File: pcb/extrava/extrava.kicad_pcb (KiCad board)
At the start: 2 copper layers, 38.1 x 40.6 mm, 24 parts, among them J1 Conn_01x01_Socket, J2 Conn_01x01_Socket, J3 Conn_01x01_Socket, J4 Conn_01x01_Socket, U1 XIAO_ESP32C3, U2 AD5941BCPZ, Y1 ABM8-16.000MHZ-10-1-U-T

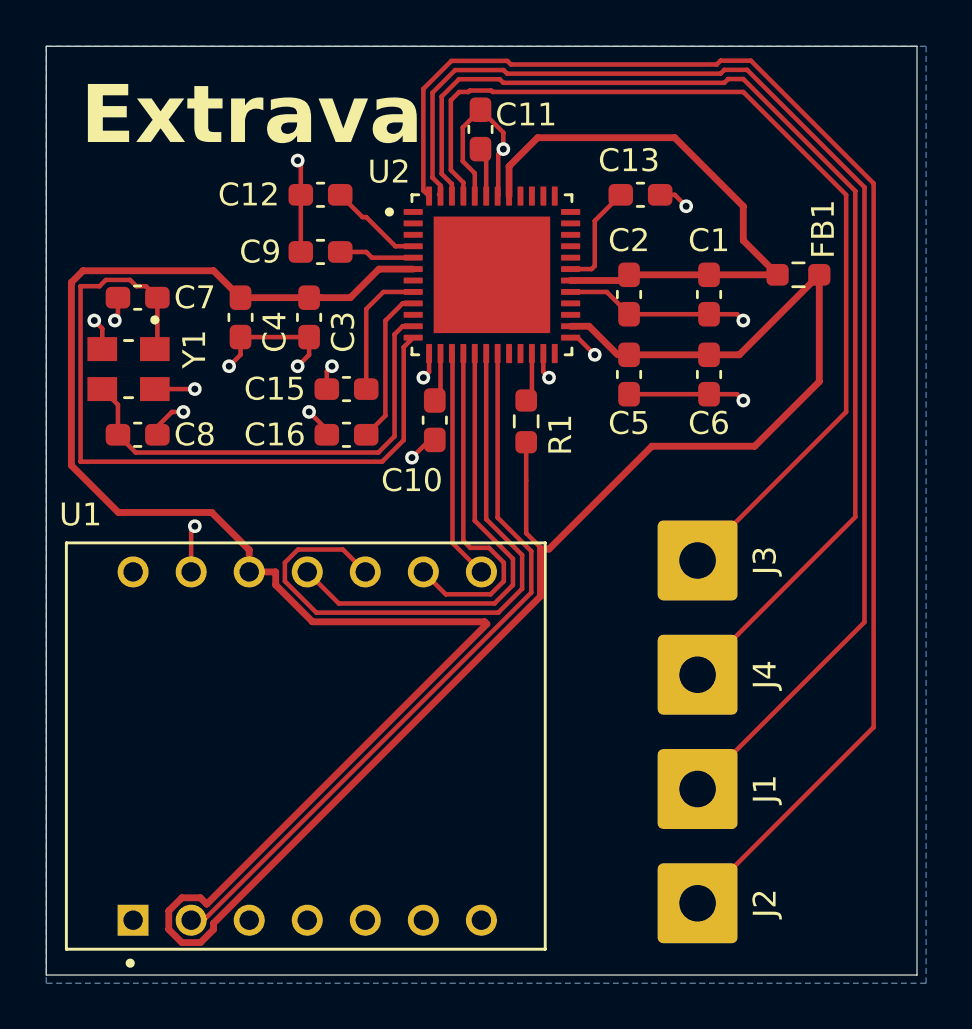
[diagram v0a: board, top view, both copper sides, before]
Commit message: fix(layout): closer decoupling caps
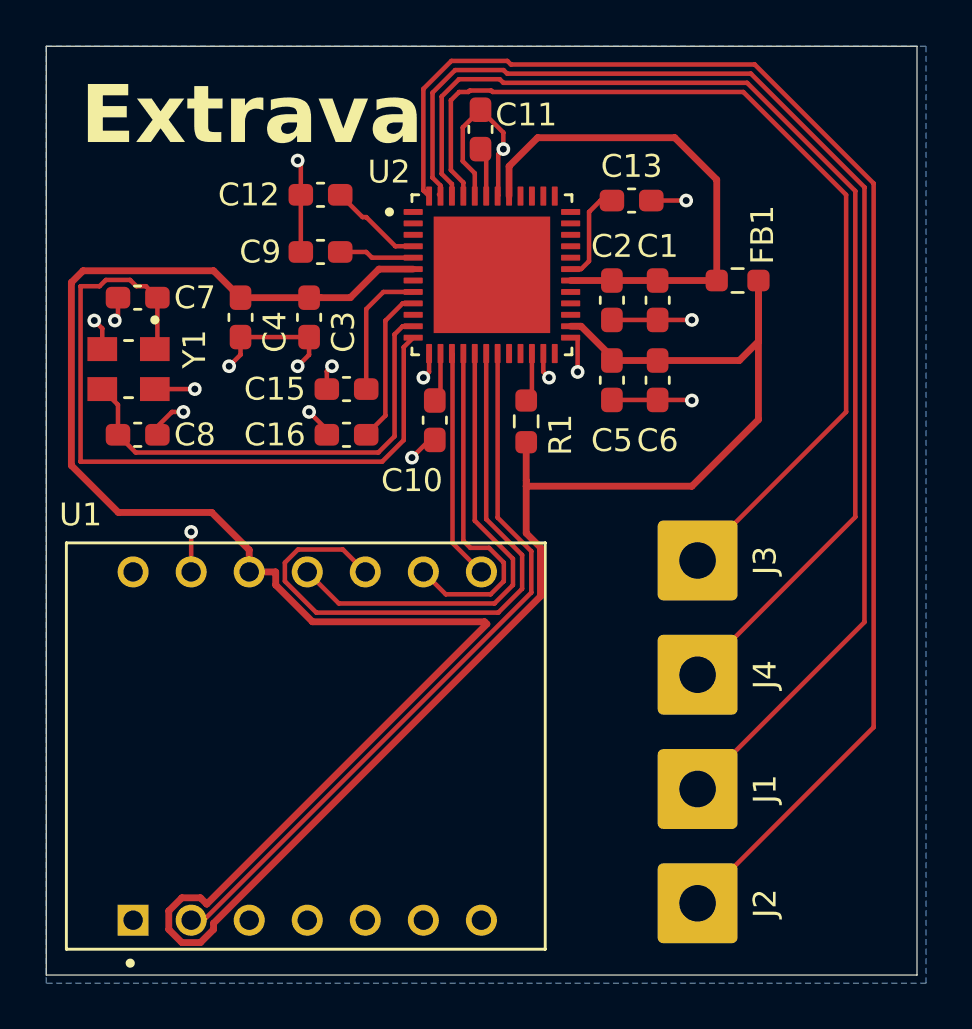
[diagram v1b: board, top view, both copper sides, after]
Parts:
- moved FB1 2.67 mm to (113.5, 53.0)
- moved C1 2.26 mm to (110.0, 53.9)
- moved C6 2.26 mm to (110.0, 57.4)
- moved C2 0.79 mm to (108.0, 53.9)
- moved C5 0.79 mm to (108.0, 57.4)
- moved C13 0.46 mm to (108.9, 49.5)
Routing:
- net GND: track 48.6 -> 42.7 mm
- net AVDD: track 26.1 -> 22.5 mm
- net +3.3V: track 128.8 -> 125.4 mm

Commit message: feat: added velostat to system
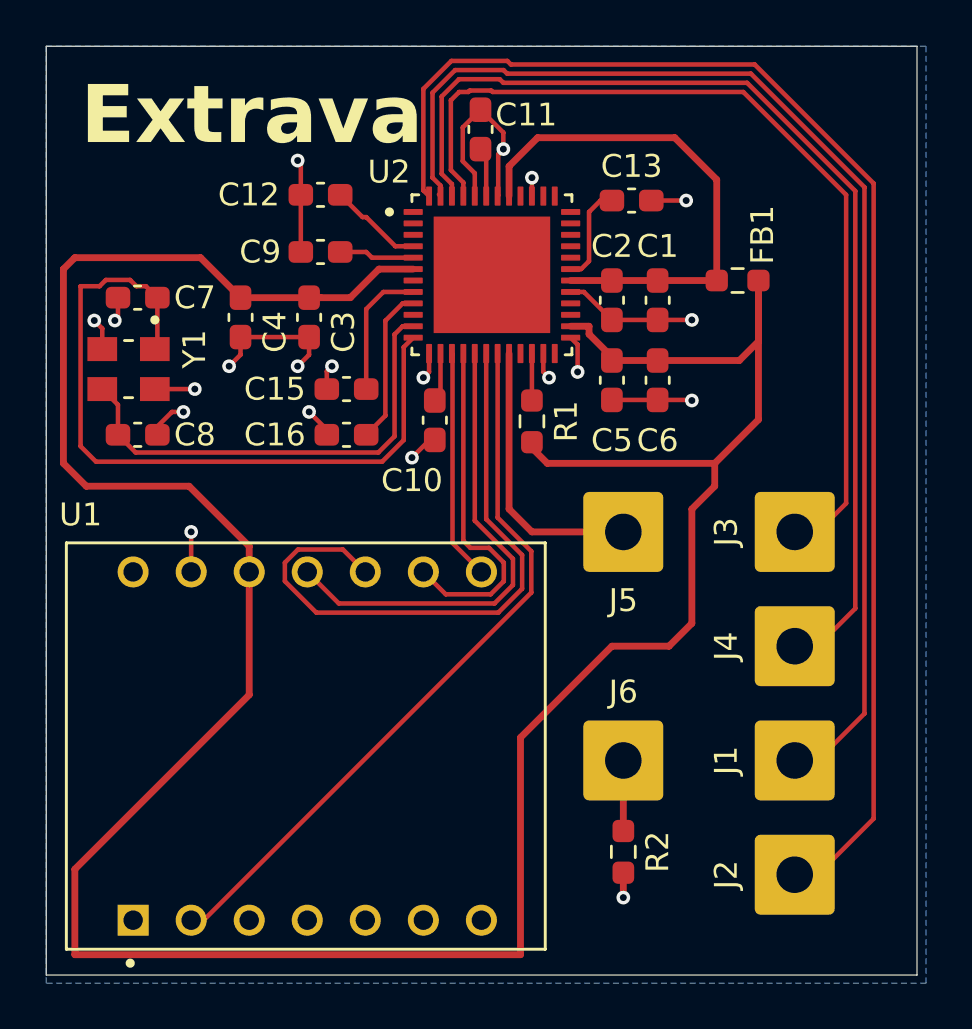
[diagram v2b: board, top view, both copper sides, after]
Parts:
- added J5: Conn_01x01_Socket, Connector_Wire:SolderWire-0.75sqmm_1x01_D1.25mm_OD3.5mm, F.Cu at (108.5, 64.0)
- added J6: Conn_01x01_Socket, Connector_Wire:SolderWire-0.75sqmm_1x01_D1.25mm_OD3.5mm, F.Cu at (108.5, 74.0)
- added R2: 10kR, Resistor_SMD:R_0603_1608Metric_Pad0.98x0.95mm_HandSolder, F.Cu at (108.5, 78.0)
- moved J1 4.43 mm to (116.0, 74.0)
- moved J2 4.43 mm to (116.0, 79.0)
- moved J3 4.43 mm to (116.0, 64.0)
- moved J4 4.43 mm to (116.0, 69.0)
- moved R1 0.25 mm to (104.5, 59.2)
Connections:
- U2 pad 20: unconnected-(U2-GPIO1-Pad20) -> VELOSTAT+
- U2 pad 39: unconnected-(U2-AIN0-Pad39) -> GND
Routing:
- net VELOSTAT+: track 0.00 -> 12.2 mm
- net +3.3V: track 125.4 -> 131.1 mm
- net GND: track 42.7 -> 46.8 mm, vias 18 -> 20
- net VELOSTAT-: track 0.00 -> 3.09 mm
- net VOLT+: track 61.9 -> 59.0 mm
- net CURR+: track 55.6 -> 53.1 mm
- net VOLT-: track 49.0 -> 46.6 mm
- net CURR-: track 42.5 -> 40.0 mm

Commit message: chore: tiddy wire traces
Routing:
- net OSC_IN: track 32.6 -> 33.1 mm
- net +3.3V: track 131.1 -> 130.5 mm
